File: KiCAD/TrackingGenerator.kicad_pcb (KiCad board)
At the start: 4 copper layers, 84.4 x 60.3 mm, 65 parts, among them IC1 ABA-52563-BLKG, IC2 ABA-52563-BLKG, IC3 ABA-52563-BLKG, J1 Conn_Coaxial, J2 Conn_Coaxial, J3 Screw_Terminal_01x02, J4 Conn_Coaxial, M1 PAM-42, U1 L7805

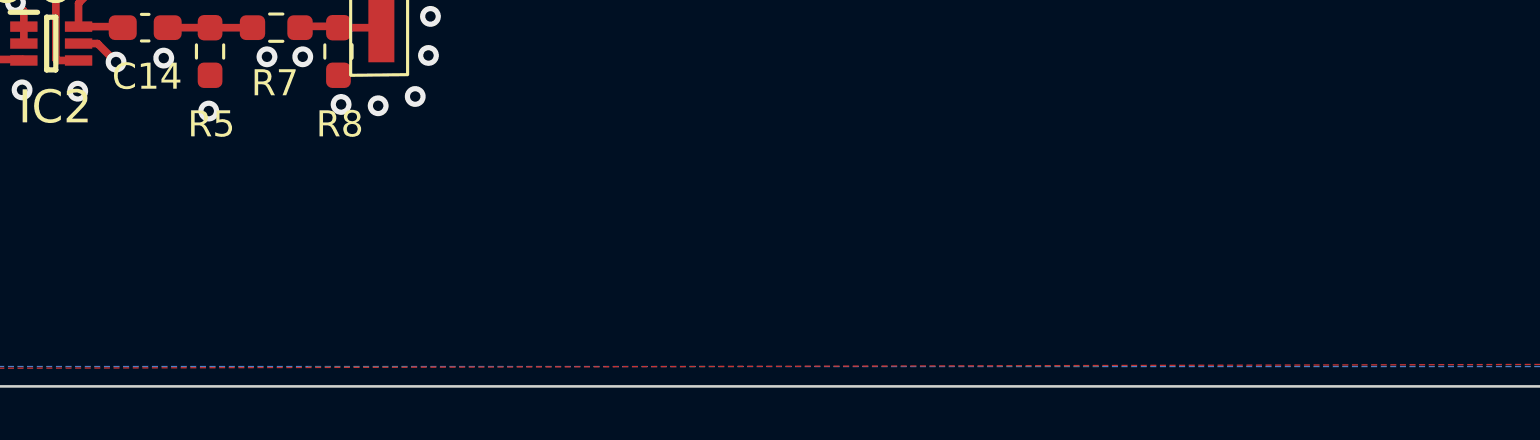
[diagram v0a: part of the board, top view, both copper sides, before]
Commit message: Added PCB text
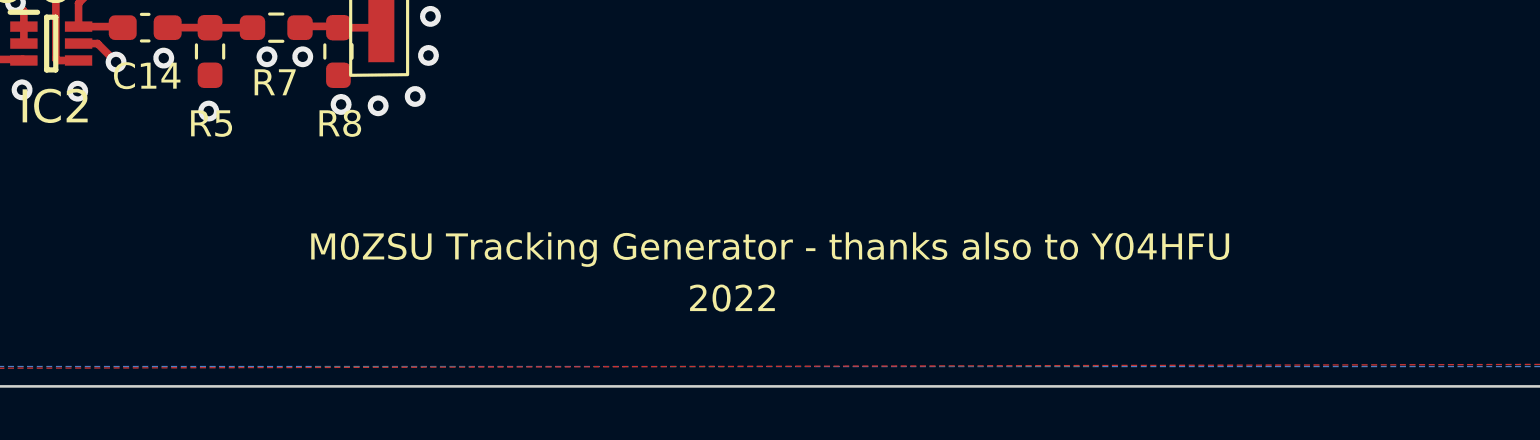
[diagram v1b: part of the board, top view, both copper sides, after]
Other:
- board text added: "2022"
- board text added: "M0ZSU Tracking Generator - thanks also to Y04HFU"
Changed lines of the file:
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@@
   )
   (gr_rect (start 70.2564 77.47) (end 154.6352 137.7696) (layer "Edge.Cuts") (width 0.1) (fill none))
+  (gr_text "2022" (at 114.2492 134.4168) (layer "F.SilkS")
+    (effects (font (size 1 1) (thickness 0.15)))
+  )
+  (gr_text "M0ZSU Tracking Generator - thanks also to Y04HFU" (at 115.6716 132.4356) (layer "F.SilkS")
+    (effects (font (size 1 1) (thickness 0.15)))
+  )
   (segment (start 87.0372 123.9624) (end 87.0372 124.6124) (width 0.29337) (layer "F.Cu") (net 1))
   (segment (start 88.0364 116.3309) (end 87.9326 116.3309) (width 0.29337) (layer "F.Cu") (net 1))

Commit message: Update Gerbers
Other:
- board text added: "and M0SKP"
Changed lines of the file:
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@@
+    (effects (font (size 1 1) (thickness 0.15)))
+  )
+  (gr_text "and M0SKP" (at 140.3604 132.4356) (layer "F.SilkS")
     (effects (font (size 1 1) (thickness 0.15)))
   )
